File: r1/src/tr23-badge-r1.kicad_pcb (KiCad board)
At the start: 4 copper layers, 111.2 x 142.3 mm, 249 parts, among them J1 532610271, J2 USB-C-12, J3 USB-A-10mm-flangeless, J4 AFC07-S40ECA-00, J5 PJ-320D, J6 2x03-socket-2.54-through-board, J7 TF-15x15, J8 DNP, Q1 MMBT3904-TP, Q2 MMBT3904-TP, Q3 MMBT3904-TP, Q4 DMG2305UX-13, Q5 DMG2305UX-13, Q6 AP2302B, SW1 REV_TACT, SW10 REV_TACT, SW11 REV_TACT, SW12 REV_TACT, SW13 REV_TACT, SW14 REV_TACT, SW15 REV_TACT, SW16 REV_TACT, SW17 REV_TACT, SW18 REV_TACT, SW19 REV_TACT, SW2 REV_TACT, SW20 REV_TACT, SW21 REV_TACT, SW22 REV_TACT, SW23 REV_TACT, SW24 REV_TACT, SW25 REV_TACT, SW26 REV_TACT, SW27 REV_TACT, SW28 REV_TACT, SW29 REV_TACT, SW3 REV_TACT, SW30 REV_TACT, SW31 REV_TACT, SW32 REV_TACT, SW33 REV_TACT, SW34 REV_TACT, SW4 REV_TACT, SW5 REV_TACT, SW6 REV_TACT, SW7 REV_TACT, SW8 REV_TACT, SW9 REV_TACT, U1 MCP73831T-2ACI_OT, U2 AP2114H-3_3TRG1, U3 CP2102N-A01-GQFN24, U4 PCM5100APW, U5 PAM8908, U6 PCA9555PW, U7 PCA9555PW, U8 PCA9555PW, U9 CC1200, Y1 32.768kHz, Y2 40Mhz

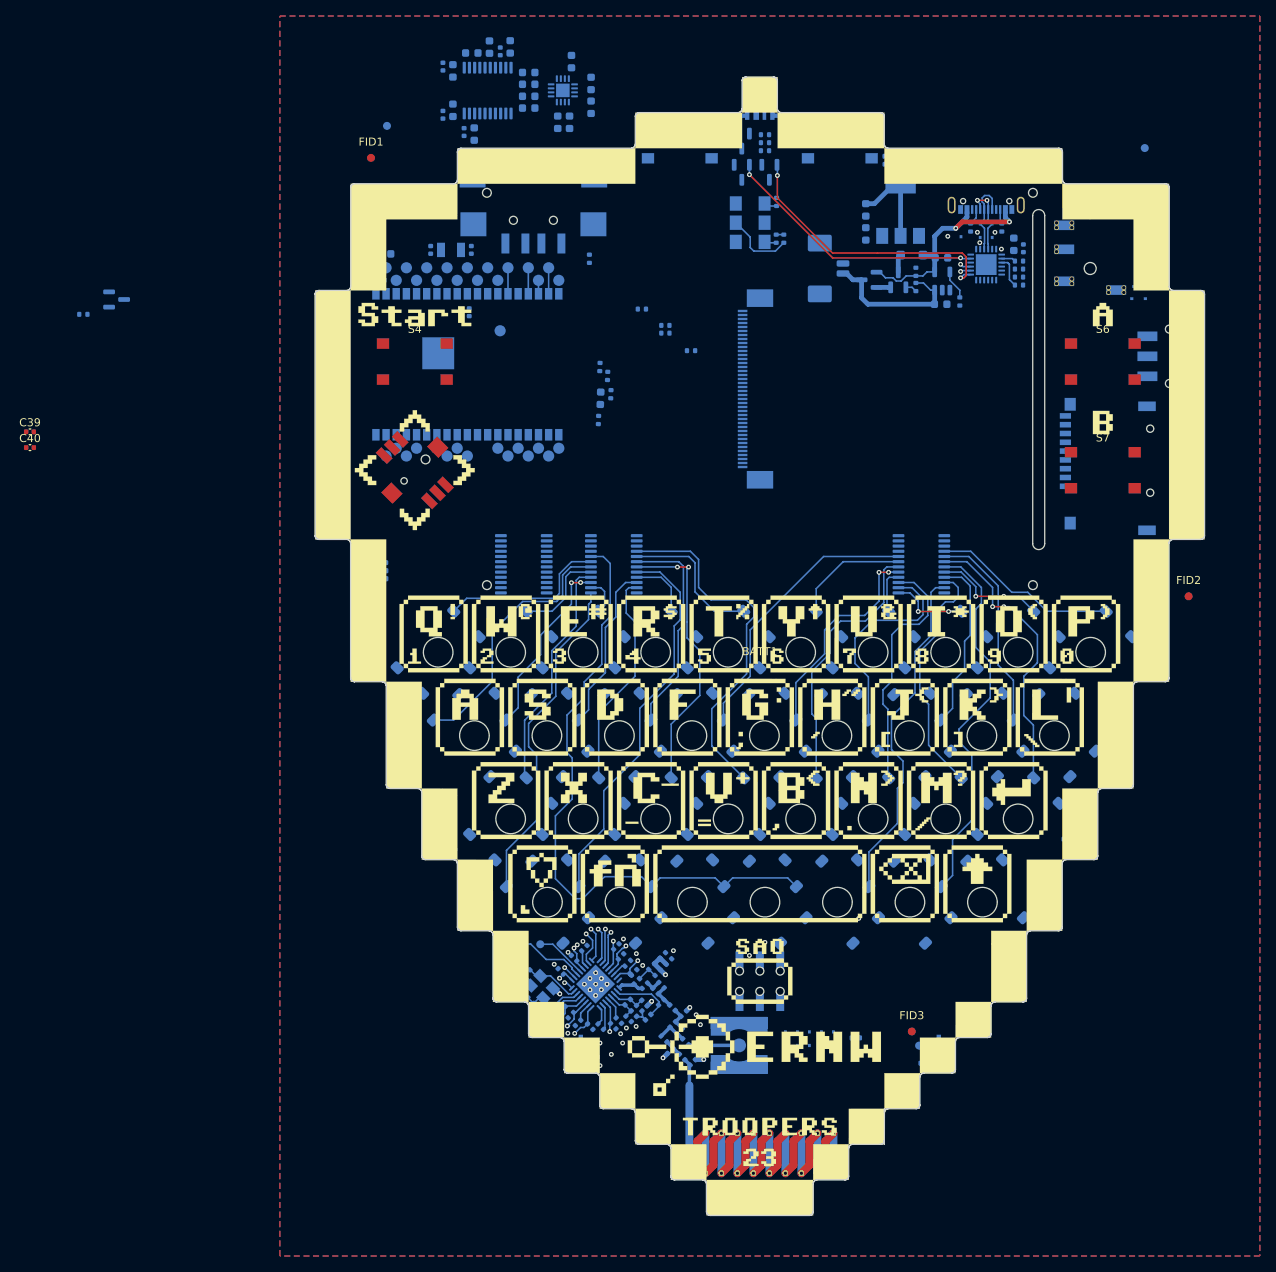
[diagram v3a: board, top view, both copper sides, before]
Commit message: Correct display connector position. Route SD bus
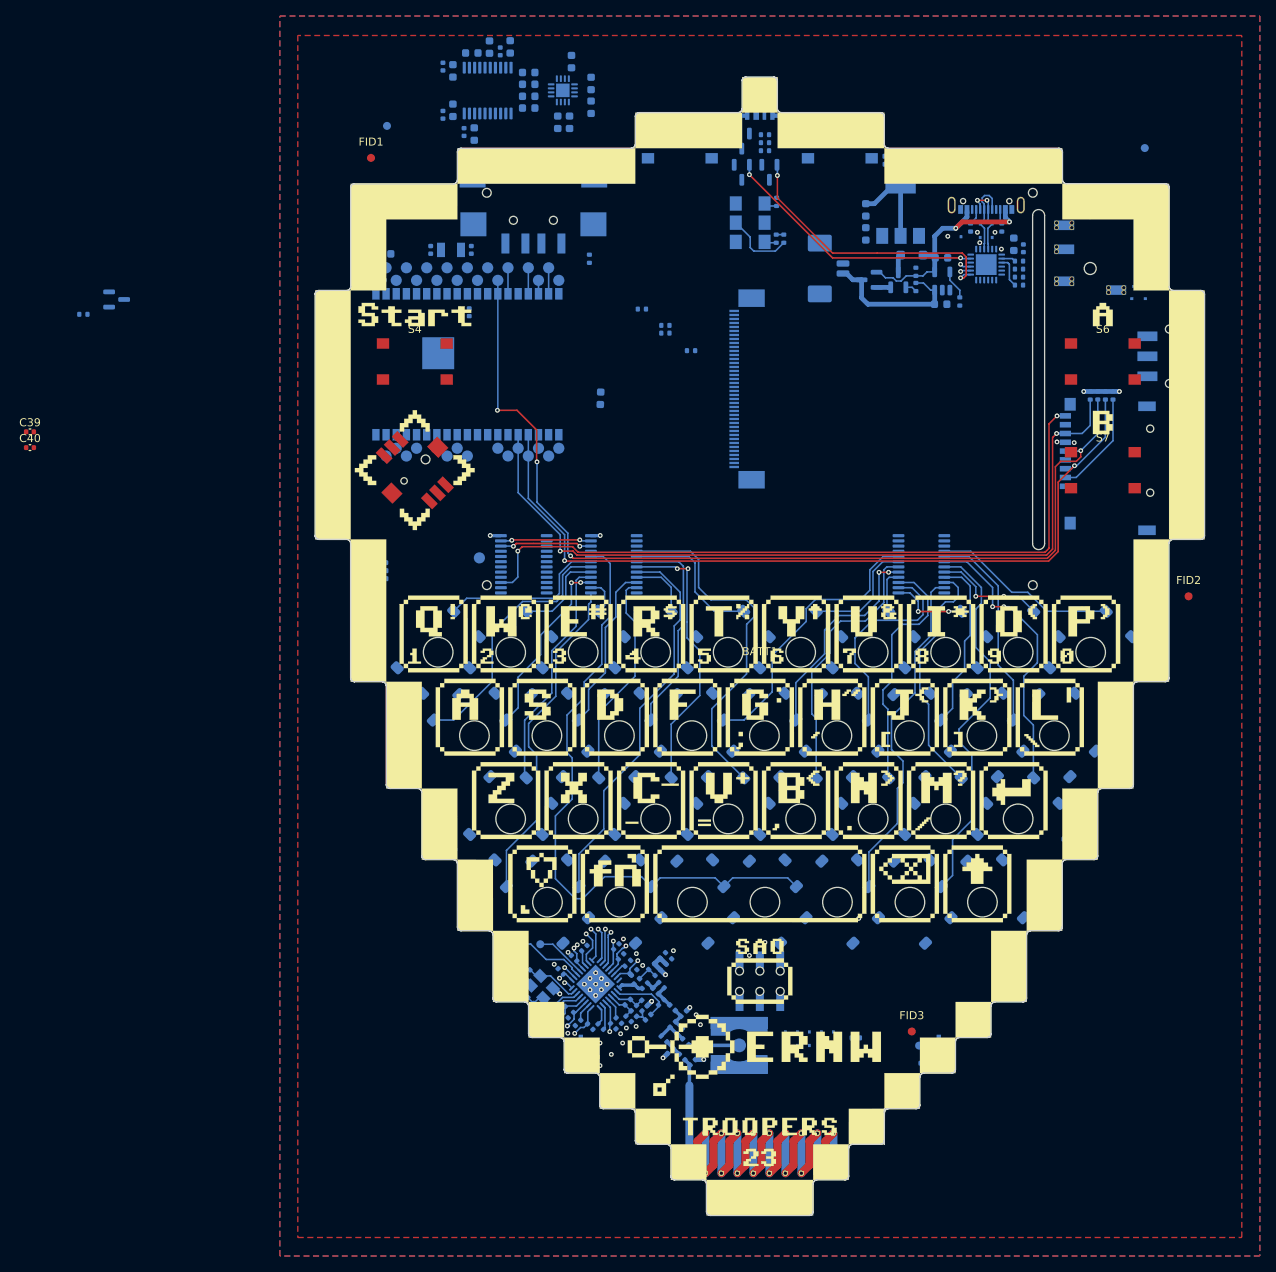
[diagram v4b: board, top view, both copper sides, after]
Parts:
- moved R25 64.2 mm to (44.1, -102.5), turned to -90 degrees
- moved R22 62.3 mm to (43.2, -102.5), turned to -90 degrees
- moved R24 61.5 mm to (41.3, -102.5), turned to -90 degrees
- moved R23 60.9 mm to (42.2, -102.5), turned to -90 degrees
- moved TP33 28.5 mm to (-35.0, -82.2)
- moved J4 1.05 mm to (-1.85, -103.3)
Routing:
- net /SD_CLK: track 0.00 -> 125.0 mm, vias 0 -> 4
- net /SD_CMD: track 0.00 -> 102.7 mm, vias 0 -> 2
- net /SD_DAT0: track 0.00 -> 102.4 mm, vias 0 -> 2
- net /SD_DETECT: track 0.00 -> 90.8 mm, vias 0 -> 2
- net Net-(J7-DAT3/CD): track 0.00 -> 13.0 mm
- net /SCL: track 0.00 -> 11.6 mm, vias 1 -> 3
- net /SDA: track 0.00 -> 11.4 mm, vias 2 -> 4
- net +3.3V: track 49.8 -> 56.8 mm, vias 13 -> 17
- net GND: vias 38 -> 40
- added copper zone on F.Cu, net +3.3V
